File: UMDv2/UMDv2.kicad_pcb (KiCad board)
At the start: 2 copper layers, 104.1 x 83.8 mm, 79 parts, among them CON201 10118194-0001LF, CON301 USB-B1HSB6, CON302 PIC_ICSP, CON303 101-00405-75, CON304 UMDv2-CONN, Q201 SMMBT3904LT1G, U201 MIC5504-3.3YM5-TR, U202 TPS2115APWR, U203 AP22802BW5-7, U204 AP22802BW5-7, U205 AZ1117CH-3.3TRG1, U206 AP22802BW5-7, U207 INA199A2DCKR, U301 PIC32MX795F512LT-80I/PF, U302 74ALVC164245DL,118, U303 74ALVC164245DL,118, U304 SN74AHC16373DLR, U305 S25FL127SABMFI101, X301 ECS-80-18-30-JGN-TR

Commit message: ajsfasfasfkihjasd;fkj
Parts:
- added D305: LO_M67K-K2M1-24-Z, db-smt:SMD-2, F.Cu at (148.2, 130.8)
- added R307: 750, db-smt:0603, F.Cu at (148.7, 134.9)
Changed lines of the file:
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@@
     (tracks 0)
     (zones 0)
-    (modules 79)
-    (nets 174)
+    (modules 81)
+    (nets 175)
   )
   (page A4)
@@
   (net 172 "Net-(D304-Pad1)")
   (net 173 "Net-(D202-Pad1)")
+  (net 174 "Net-(D305-Pad1)")
   (net_class Default "This is the default net class."
     (clearance 0.2)
@@
     (add_net "Net-(D202-Pad1)")
     (add_net "Net-(D304-Pad1)")
+    (add_net "Net-(D305-Pad1)")
     (add_net "Net-(Q201-Pad1)")
     (add_net "Net-(Q201-Pad3)")
@@
   )
   (module db-smt:0603 (layer F.Cu)
+    (at 148.69414 134.85114)
+    (tags 0603)
+    (solder_mask_margin 0.1016)
+    (attr smd)
+    (fp_text reference R307 (at 0.12954 -1.23698) (layer F.SilkS)
+      (effects (font (size 0.889 0.889) (thickness 0.2032)))
+    )
+    (fp_text value 750 (at 0.508 -2.54) (layer F.Fab) hide
+      (effects (font (size 1 1) (thickness 0.15)))
+    )
+    (fp_line (start 0 -0.381) (end 0 0.381) (layer F.SilkS) (width 0.254))
+    (pad 1 smd rect (at -0.95 0) (size 0.8 1) (layers F.Cu F.Paste F.Mask)
+      (net 1 GND))
+    (pad 2 smd rect (at 0.95 0) (size 0.8 1) (layers F.Cu F.Paste F.Mask)
+      (net 174 "Net-(D305-Pad1)"))
+    (model Resistors_SMD.3dshapes/R_0603.wrl
+      (at (xyz 0 0 0))
+      (scale (xyz 1 1 1))
+      (rotate (xyz 0 0 0))
+    )
+  )
+  (module db-smt:SMD-2 (layer F.Cu)
+    (at 148.20392 130.7846)
+    (solder_mask_margin 0.1016)
+    (fp_text reference D305 (at 1.23698 -1.6256) (layer F.SilkS)
+      (effects (font (size 0.889 0.889) (thickness 0.2032)))
+    )
+    (fp_text value LO_M67K-K2M1-24-Z (at -1.6 -1.8) (layer F.Fab) hide
+      (effects (font (size 0.889 0.889) (thickness 0.2032)))
+    )
+    (fp_line (start -0.2 0.8) (end 2 0.8) (layer F.SilkS) (width 0.254))
+    (fp_line (start 0.4 -0.8) (end 2 -0.8) (layer F.SilkS) (width 0.254))
+    (pad 1 smd rect (at 0 0) (size 1 1) (layers F.Cu F.Paste F.Mask)
+      (net 174 "Net-(D305-Pad1)"))
+    (pad 2 smd rect (at 1.8 0) (size 1 1) (layers F.Cu F.Paste F.Mask)
+      (net 169 /Microcontroller/BOOT_LED))
+  )
+  (module db-smt:0603 (layer F.Cu)
     (at 114.20602 74.85634 180)
     (tags 0603)
@@
     (at 180.2765 64.3636)
     (solder_mask_margin 0.1016)
-    (fp_text reference CON304 (at 2.54 -3.175) (layer F.SilkS)
-      (effects (font (size 0.889 0.889) (thickness 0.2032)))
-    )
+    (fp_text reference CON304 (at 4.33578 -0.5461) (layer F.SilkS)
+      (effects (font (size 0.889 0.889) (thickness 0.2032)))
+    )

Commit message: lots of parts placement
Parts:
- added C308: 0.1uF/50V, db-smt:0603, F.Cu at (137.6, 137.0)
- added C309: 0.1uF/50V, db-smt:0603, F.Cu at (177.9, 68.4)
- added C310: 0.1uF/50V, db-smt:0603, F.Cu at (176.5, 141.3)
- added C311: 10uF/16V, db-smt:0805, F.Cu at (175.3, 143.8)
- added C312: 0.1uF/50V, db-smt:0603, F.Cu at (177.9, 65.0)
- added R308: 10.0k, db-smt:0603, F.Cu at (101.1, 131.3)
- added SW301: PTS645SM43SMTR92_LFS, db-smt:PTS645, F.Cu at (108.1, 137.6)
- added SW302: PTS645SM43SMTR92_LFS, db-smt:PTS645, F.Cu at (99.7, 137.6)
- added TP201: TP_50, db-smt:TP50, F.Cu at (124.3, 64.3)
- added TP202: TP_50, db-smt:TP50, F.Cu at (124.4, 66.4)
- added TP203: TP_50, db-smt:TP50, F.Cu at (126.6, 87.2)
- added TP204: TP_50, db-smt:TP50, F.Cu at (126.6, 83.2)
- added TP205: TP_50, db-smt:TP50, F.Cu at (124.4, 68.4)
- added TP206: TP_50, db-smt:TP50, F.Cu at (157.9, 80.3)
- added TP301: TP_50, db-smt:TP50, F.Cu at (126.6, 85.2)
- moved C212 9.93 mm to (151.9, 66.1), turned to 180 degrees
- moved D201 9.90 mm to (148.5, 79.1), turned to 270 degrees
- moved R206 9.49 mm to (147.3, 75.5), turned to 270 degrees
- moved R207 9.40 mm to (154.5, 75.1)
- moved R208 7.18 mm to (152.4, 79.1), turned to 180 degrees
- moved C210 6.12 mm to (124.3, 79.2)
- moved C307 6.04 mm to (131.3, 124.6)
- moved C208 6.02 mm to (127.9, 71.9)
- moved U305 5.92 mm to (124.0, 126.2)
- moved U207 5.69 mm to (152.2, 69.7), turned to 180 degrees
- moved C211 5.03 mm to (148.0, 66.1), turned to 0 degrees
- moved U205 4.52 mm to (133.8, 71.1)
- moved C206 4.34 mm to (130.1, 77.0)
- moved D303 4.26 mm to (173.0, 71.2), turned to 180 degrees
- moved C209 4.24 mm to (137.0, 77.0)
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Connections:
- net Net-(U303-Pad46) renamed /Microcontroller/~RST~
- U301 pad 19: Net-(U301-Pad19) -> /Microcontroller/~UCART~
- U301 pad 28: Net-(U301-Pad28) -> /Microcontroller/~GOE~
- U301 pad 29: Net-(U301-Pad29) -> /Microcontroller/~AOE~
- U301 pad 42: /Microcontroller/~AOE~ -> Net-(U301-Pad42)
- U301 pad 68: Net-(U301-Pad68) -> /Microcontroller/~DOEH~
- U301 pad 69: Net-(U301-Pad69) -> /Microcontroller/DIRH
- U301 pad 77: /Microcontroller/~DOE~ -> /Microcontroller/~DOEL~
- U301 pad 78: /Microcontroller/DIR -> /Microcontroller/DIRL
- U302 pad 1: /Microcontroller/DIR -> /Microcontroller/DIRL
- U302 pad 24: /Microcontroller/DIR -> /Microcontroller/DIRH
- U302 pad 25: /Microcontroller/~DOE~ -> /Microcontroller/~DOEH~
- U302 pad 48: /Microcontroller/~DOE~ -> /Microcontroller/~DOEL~
- U303 pad 3: Net-(U303-Pad3) -> /Microcontroller/~URST~
- U303 pad 48: Net-(U303-Pad48) -> /Microcontroller/~GOE~
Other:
- board text added: "16MB Flash"
- board text added: "3.3VP"
- board text added: "3V3"
- board text added: "5V"
- board text added: "5VD"
- board text added: "PRG"
- board text added: "RST"
- board text added: "USB Power"
- board text added: "VDD"
- board text added: "Vsec"
- board text removed: "USB Secondary Power"

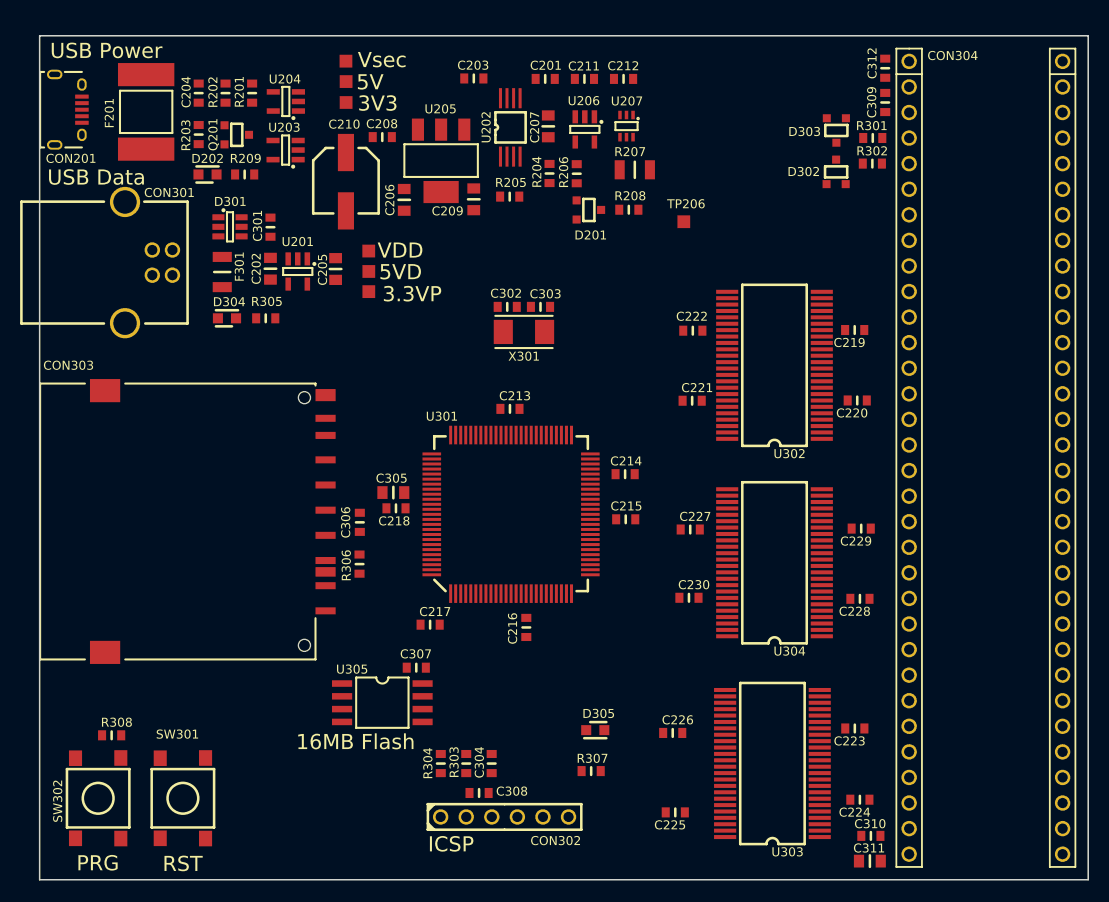
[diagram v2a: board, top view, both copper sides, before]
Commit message: routing the power supply section
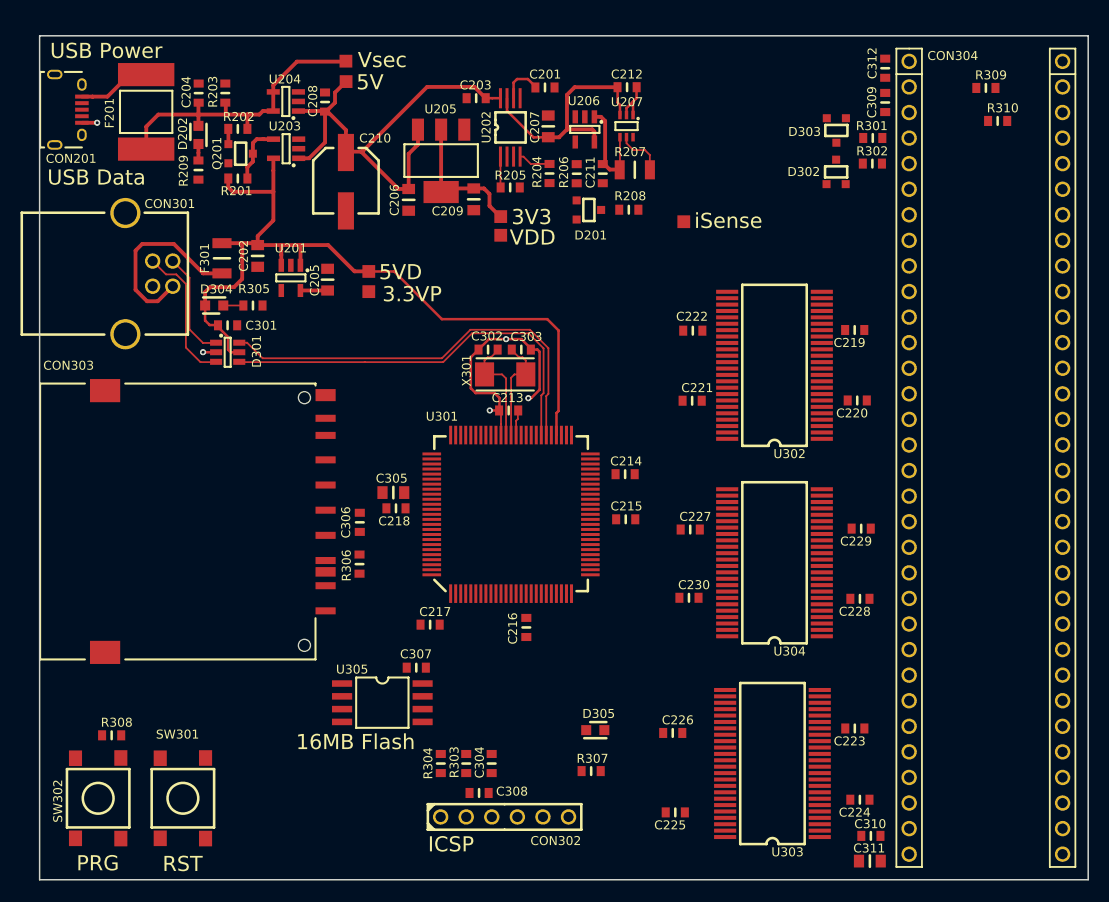
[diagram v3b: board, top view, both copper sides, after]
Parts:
- added R309: 2.20k, db-smt:0603, F.Cu at (187.9, 67.0)
- added R310: 2.20k, db-smt:0603, F.Cu at (189.1, 70.3)
- moved TP205 19.1 mm to (139.7, 79.8)
- moved TP204 13.2 mm to (139.7, 81.6)
- moved D301 12.5 mm to (111.4, 92.3)
- moved C301 10.6 mm to (112.6, 90.6), turned to 0 degrees
- moved C211 9.58 mm to (149.8, 75.5), turned to 90 degrees
- moved R201 8.60 mm to (113.6, 76.0), turned to 0 degrees
- moved C208 6.67 mm to (122.3, 68.4), turned to 270 degrees
- moved R203 4.90 mm to (112.4, 67.5), turned to 90 degrees
- moved C302 4.65 mm to (138.5, 93.0)
- moved C303 4.65 mm to (141.8, 93.0)
- moved X301 4.61 mm to (142.2, 95.5)
- moved R209 4.61 mm to (109.7, 75.2), turned to 90 degrees
- moved R202 3.76 mm to (113.6, 71.1), turned to 180 degrees
- moved D202 3.52 mm to (109.7, 72.6), turned to 90 degrees
- moved C203 1.98 mm to (137.3, 68.0)
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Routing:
- net +5VD: track 0.00 -> 82.2 mm
- net +5V: track 0.00 -> 48.6 mm
- net /Microcontroller/D-: track 0.00 -> 42.0 mm
- net /Microcontroller/D+: track 0.00 -> 40.8 mm
- net GND: track 0.00 -> 31.8 mm, vias 0 -> 5
- net /Power Section/Vsec: track 0.00 -> 31.0 mm
- net VDD: track 0.00 -> 24.0 mm
- net /Microcontroller/Vbus: track 0.00 -> 19.2 mm
- net +3V3: track 0.00 -> 18.2 mm
- net /Microcontroller/D+in: track 0.00 -> 14.1 mm
- net Net-(C302-Pad1): track 0.00 -> 11.1 mm
- net /Microcontroller/D-in: track 0.00 -> 10.7 mm
- net Net-(C303-Pad1): track 0.00 -> 10.5 mm
- net /Power Section/RS+: track 0.00 -> 10.4 mm
- net Net-(CON201-Pad1): track 0.00 -> 7.27 mm
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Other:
- net class Default: clearance 0.2 -> 0.1778; trace_width 0.25 -> 0.1778; via_dia 0.6 -> 0.6096; via_drill 0.4 -> 0.3048
- net class Power added: clearance 0.1778, trace_width 0.254, via_dia 0.6096, via_drill 0.3048
- rule pad_to_mask_clearance: 0.2 -> 0.1016
- rule trace_clearance: 0.2 -> 0.1778
- rule trace_min: 0.2 -> 0.1778
- rule via_min_drill: 0.3 -> 0.3048
- rule via_min_size: 0.4 -> 0.6096
- board text added: "iSense"

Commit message: bit of work
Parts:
- moved TP206 18.4 mm to (139.7, 83.5)
- moved R208 5.51 mm to (154.2, 73.9)
- moved D201 2.60 mm to (151.1, 79.1)
- moved R207 1.07 mm to (155.3, 75.9)
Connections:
- U301 pad 73: Net-(U301-Pad73) -> /Microcontroller/CVEN
- U301 pad 74: Net-(U301-Pad74) -> /Microcontroller/5V/~3V~
- U301 pad 96: /Microcontroller/CVEN -> Net-(U301-Pad96)
- U301 pad 97: /Microcontroller/5V/~3V~ -> Net-(U301-Pad97)
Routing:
- net /Microcontroller/iSense: track 0.00 -> 20.3 mm
- net VDD: track 24.0 -> 39.0 mm
- net GND: track 31.8 -> 27.2 mm
- net Net-(R208-Pad1): track 0.00 -> 3.56 mm
- net /Power Section/RS+: track 10.4 -> 13.5 mm
- net /Microcontroller/CVEN: track 0.00 -> 2.26 mm
- net VCC: track 4.82 -> 6.04 mm

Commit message: just routing
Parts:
- added C231: 10uF/16V, db-smt:0805, F.Cu at (130.1, 97.5)
- moved U305 11.4 mm to (112.6, 126.3)
- moved C307 8.71 mm to (123.0, 127.2), turned to 90 degrees
- moved R308 1.55 mm to (102.4, 132.1)
- moved C217 1.29 mm to (134.0, 120.1)
- moved SW301 0.81 mm to (107.6, 138.2)
- moved SW302 0.81 mm to (99.2, 138.2)
- moved C306 0.41 mm to (125.4, 109.9)
- moved R306 0.36 mm to (125.4, 114.1)
- moved C216 0.16 mm to (142.1, 120.6)
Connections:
- U301 pad 1: /Microcontroller/~SSSF~ -> /Microcontroller/~SDCD~
- U301 pad 18: /Microcontroller/~SDCD~ -> /Microcontroller/~SSSF~
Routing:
- net +3.3VP: track 5.09 -> 93.6 mm, vias 0 -> 5
- net /Microcontroller/SDI2: track 0.00 -> 66.9 mm
- net /Microcontroller/SCK2: track 0.00 -> 59.6 mm
- net GND: track 27.2 -> 85.2 mm, vias 5 -> 27
- net /Microcontroller/SDO2: track 0.00 -> 54.1 mm, vias 0 -> 2
- net /Microcontroller/~MCLR~: track 0.00 -> 25.1 mm
- net /Microcontroller/~SDCD~: track 0.00 -> 13.5 mm
- net /Microcontroller/~SSSD~: track 0.00 -> 8.81 mm
- net Net-(C305-Pad2): track 0.00 -> 3.13 mm
- net /Microcontroller/A16: track 0.00 -> 1.62 mm, vias 0 -> 1
- net /Microcontroller/~SSSF~: track 0.00 -> 1.32 mm
- added copper zone on B.Cu, net GND
- added copper zone on F.Cu, net GND

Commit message: routing
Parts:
- moved C217 1.49 mm to (132.7, 119.3)
- moved C307 1.22 mm to (123.7, 126.2), turned to 180 degrees
- moved C216 0.84 mm to (142.0, 121.5)
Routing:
- net /Microcontroller/~SSSF~: track 1.32 -> 40.9 mm, vias 0 -> 4
- net +3.3VP: track 93.6 -> 132.0 mm, vias 5 -> 8
- net GND: track 85.2 -> 89.2 mm
- net /Microcontroller/SDI2: track 66.9 -> 69.3 mm
- net /Microcontroller/A16: track 1.62 -> 2.22 mm

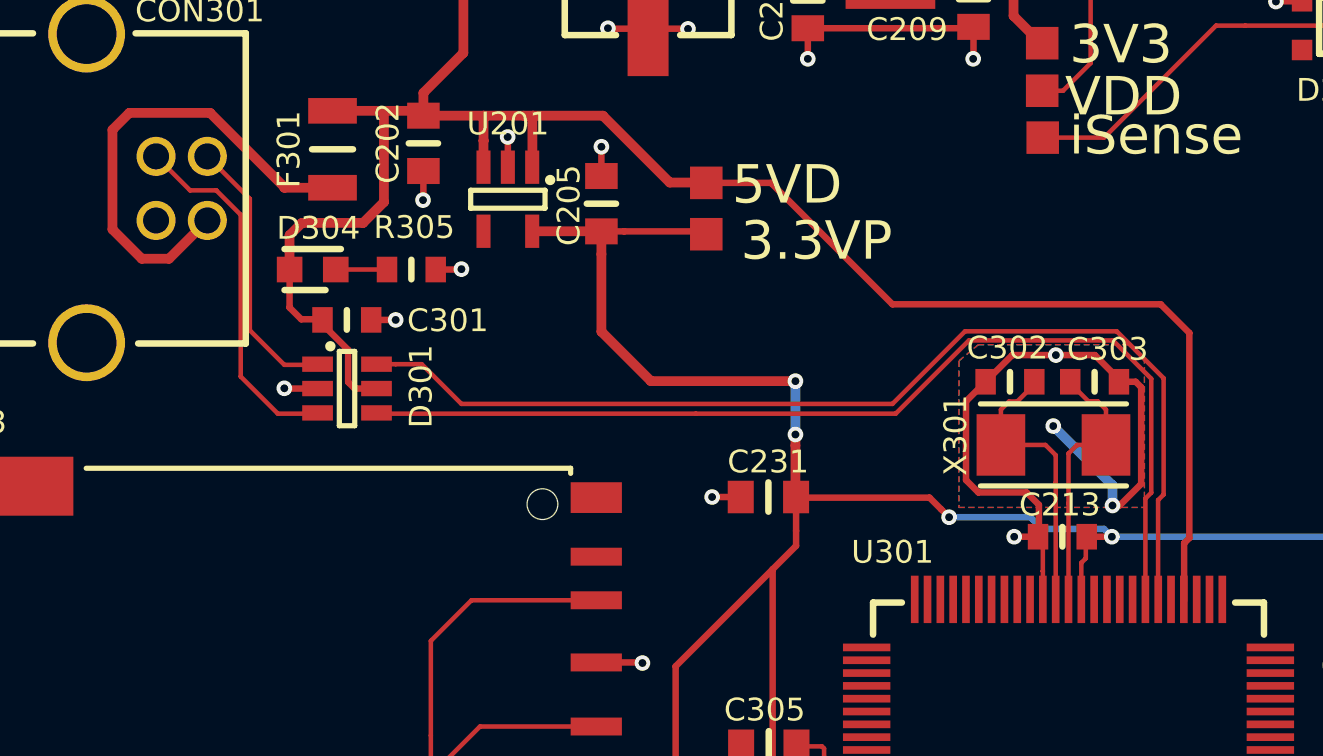
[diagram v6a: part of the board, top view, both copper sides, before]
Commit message: playing with diff routing on USB
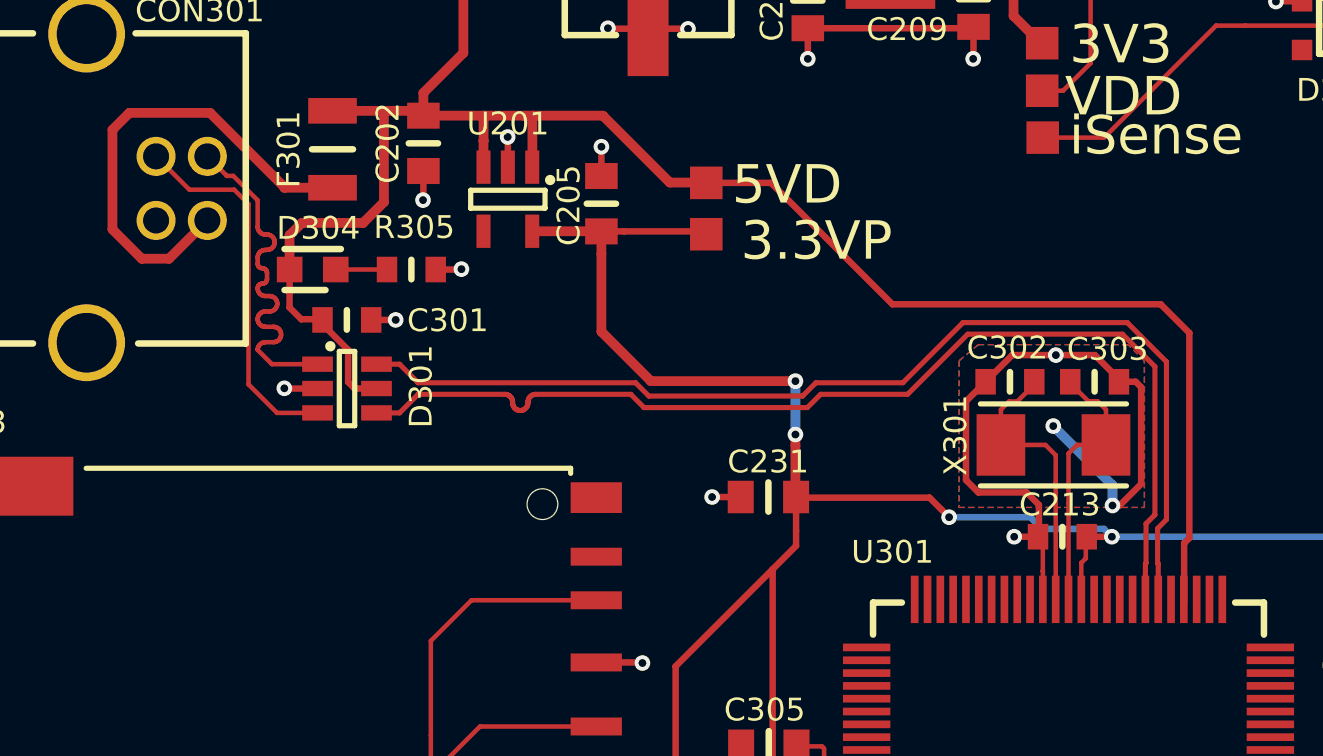
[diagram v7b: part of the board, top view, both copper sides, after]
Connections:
- net /Microcontroller/D+in renamed /Microcontroller/Din+
- net /Microcontroller/D-in renamed /Microcontroller/Din-
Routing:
- net /Microcontroller/Din-: track 10.7 -> 15.9 mm
- net /Microcontroller/D+: track 40.8 -> 42.6 mm
- net /Microcontroller/D-: track 42.0 -> 42.6 mm

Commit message: routing some PCB
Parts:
- moved R307 19.9 mm to (132.7, 123.0)
- moved TP206 16.1 mm to (155.3, 79.2)
- moved D305 14.6 mm to (135.9, 123.0)
- moved TP204 2.07 mm to (139.9, 79.6)
- moved TP205 1.84 mm to (139.9, 81.6)
- moved C225 1.64 mm to (158.0, 137.6), turned to 0 degrees
- moved R310 1.29 mm to (187.8, 69.9)
- moved C226 1.24 mm to (157.9, 130.6)
- moved C222 0.81 mm to (158.0, 91.1)
- moved C221 0.75 mm to (158.0, 98.0)
- moved C227 0.59 mm to (158.0, 110.7)
- moved C230 0.43 mm to (158.0, 117.7)
- moved U304 0.21 mm to (171.4, 121.5)
- moved U302 0.20 mm to (171.4, 101.9)
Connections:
- D201 pad 2: +3.3VP -> +3V3
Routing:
- net +3V3: track 18.2 -> 126.9 mm, vias 0 -> 2
- net Net-(C304-Pad2): track 0.00 -> 52.2 mm
- net +3.3VP: track 132.0 -> 171.4 mm
- net /Microcontroller/CVEN: track 2.26 -> 40.7 mm, vias 0 -> 2
- net /Microcontroller/5V/~3V~: track 0.00 -> 34.0 mm, vias 0 -> 2
- net /Microcontroller/PGC: track 0.00 -> 33.9 mm
- net /Microcontroller/PGD: track 0.00 -> 30.6 mm
- net /Microcontroller/~SSSD~: track 8.81 -> 38.2 mm, vias 0 -> 2
- net GND: track 89.2 -> 110.4 mm, vias 27 -> 29
- net /Microcontroller/Vbus: track 19.2 -> 5.95 mm
- net /Microcontroller/iSense: track 20.3 -> 8.24 mm, vias 0 -> 1
- net /Microcontroller/BOOT_LED: track 0.00 -> 5.70 mm
- net VCC: track 6.04 -> 11.0 mm
- net Net-(D305-Pad1): track 0.00 -> 2.23 mm
- net VDD: track 39.0 -> 37.2 mm
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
